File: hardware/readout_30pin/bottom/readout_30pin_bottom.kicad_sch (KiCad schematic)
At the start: 20 parts, among them IC1 TLV9362IDDFR, IC2 ADG706BRUZ, IC8 74HC595BQ, IC9 74HC595BQ, J2 Conn_01x07_Pin, J3 Conn_01x07_Pin, J4 Conn_01x30_Pin, U7 LM2776

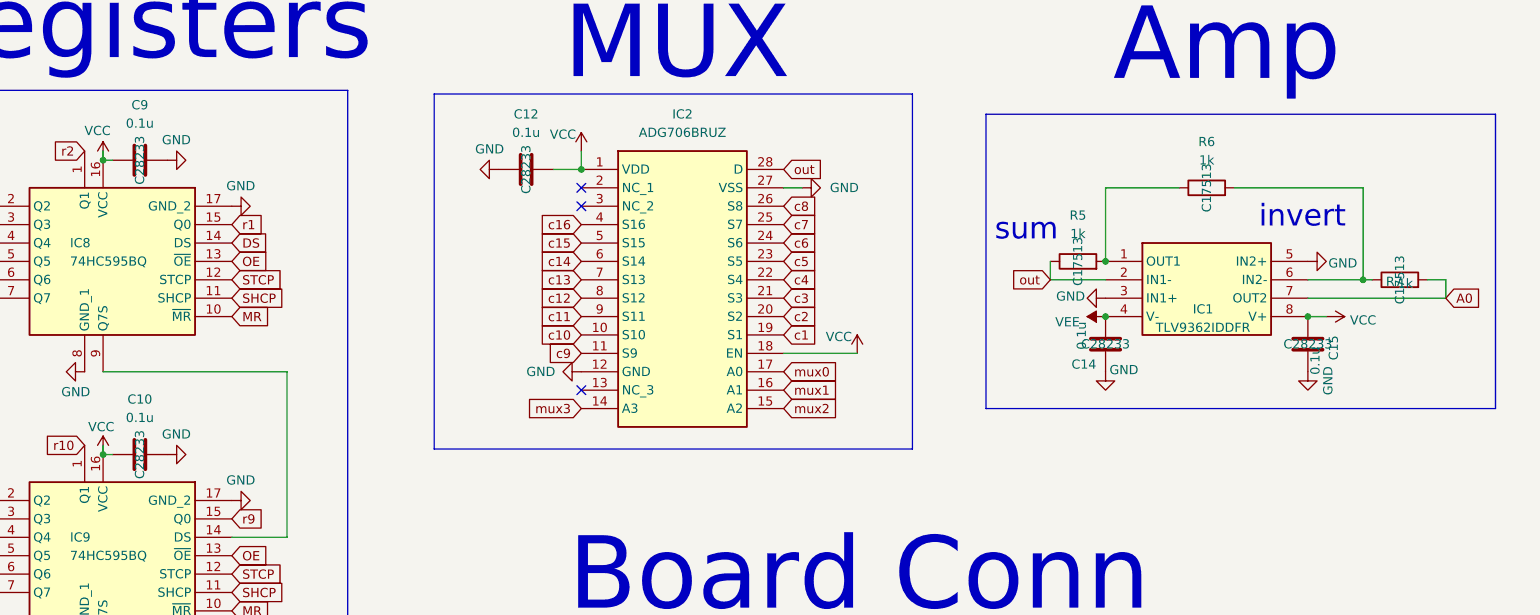
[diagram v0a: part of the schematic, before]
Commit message: Readout boards: 30-pin bottom passives on 0402 parts; 60-pin back carries a QR to opentac.github.io
From the current KiCad sources (3D model paths pointed at libs/3dmodels as
before, nothing else changed):

- 30-pin bottom (Sensor_30): the three passives listed 0805/0201 parts on 0402
  pads. Now C1525 (CL05B104KO5NNNC, 100 nF), C52923 (CL05A105KA5NQNC, 1 uF)
  and C11702 (0402WGF1001TCE, 1 kOhm), all JLCPCB Basic parts. Schematic,
  board, JLCPCB BOM, fab zip and bom.csv (MPN column) updated.
- 60-pin: back silkscreen QR code linking to opentac.github.io; board and
  fab zip re-exported.

KiCad DRC on both boards reports the same violations as before the update.
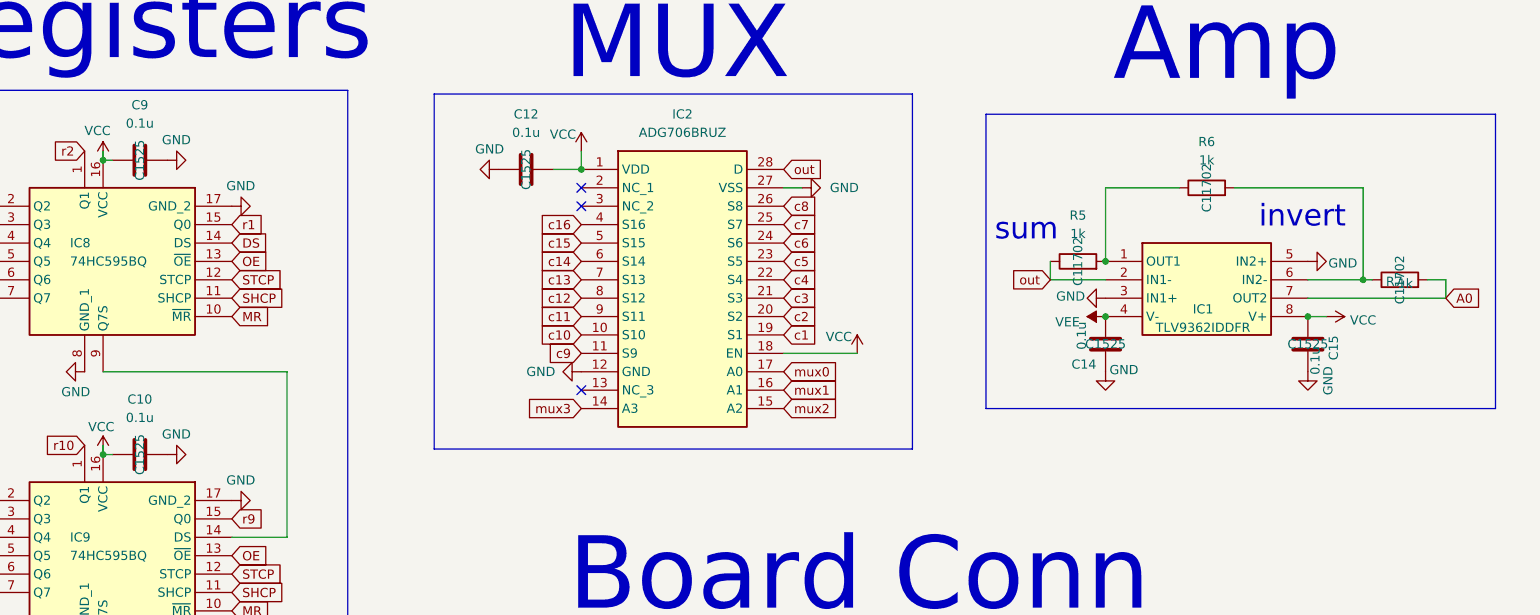
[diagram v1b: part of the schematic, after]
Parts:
- C10, C12, C14, C15, C9: LCSC Part # C28233 -> C1525
- C34, C35: LCSC Part # C53067 -> C52923
- R5, R6, R7: LCSC Part # C17513 -> C11702
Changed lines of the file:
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@@
 			)
 		)
-		(property "LCSC Part #" "C17513"
+		(property "LCSC Part #" "C11702"
 			(at 299.72 106.68 0)
 			(show_name no)
@@
 			)
 		)
-		(property "LCSC Part #" "C28233"
+		(property "LCSC Part #" "C1525"
 			(at 287.02 115.57 0)
 			(show_name no)
@@
 			)
 		)
-		(property "LCSC Part #" "C28233"
+		(property "LCSC Part #" "C1525"
 			(at 179.07 91.44 0)
 			(show_name no)
@@
 			)
 		)
-		(property "LCSC Part #" "C53067"
+		(property "LCSC Part #" "C52923"
 			(at 327.66 199.39 0)
 			(hide yes)
@@
 			)
 		)
-		(property "LCSC Part #" "C28233"
+		(property "LCSC Part #" "C1525"
 			(at 125.73 130.81 0)
 			(show_name no)
@@
 			)
 		)
-		(property "LCSC Part #" "C28233"
+		(property "LCSC Part #" "C1525"
 			(at 125.73 90.17 0)
 			(show_name no)
@@
 			)
 		)
-		(property "LCSC Part #" "C17513"
+		(property "LCSC Part #" "C11702"
 			(at 255.27 104.14 0)
 			(show_name no)
@@
 			)
 		)
-		(property "LCSC Part #" "C17513"
+		(property "LCSC Part #" "C11702"
 			(at 273.05 93.98 0)
 			(show_name no)
@@
 			)
 		)
-		(property "LCSC Part #" "C28233"
+		(property "LCSC Part #" "C1525"
 			(at 259.08 115.57 0)
 			(show_name no)
@@
 			)
 		)
-		(property "LCSC Part #" "C53067"
+		(property "LCSC Part #" "C52923"
 			(at 339.09 205.74 0)
 			(hide yes)
